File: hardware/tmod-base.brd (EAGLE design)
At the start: 65 x 56 mm, 100 parts, among them IC1 TPS70933, IC10 TPS70933, IC2 INA219SOT, IC3 STM32L052C8T6, IC4 HX1, IC5 LMP7702, IC6 TPS62143, IC8 TPS22918, IC9 BME280, J1 DNP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

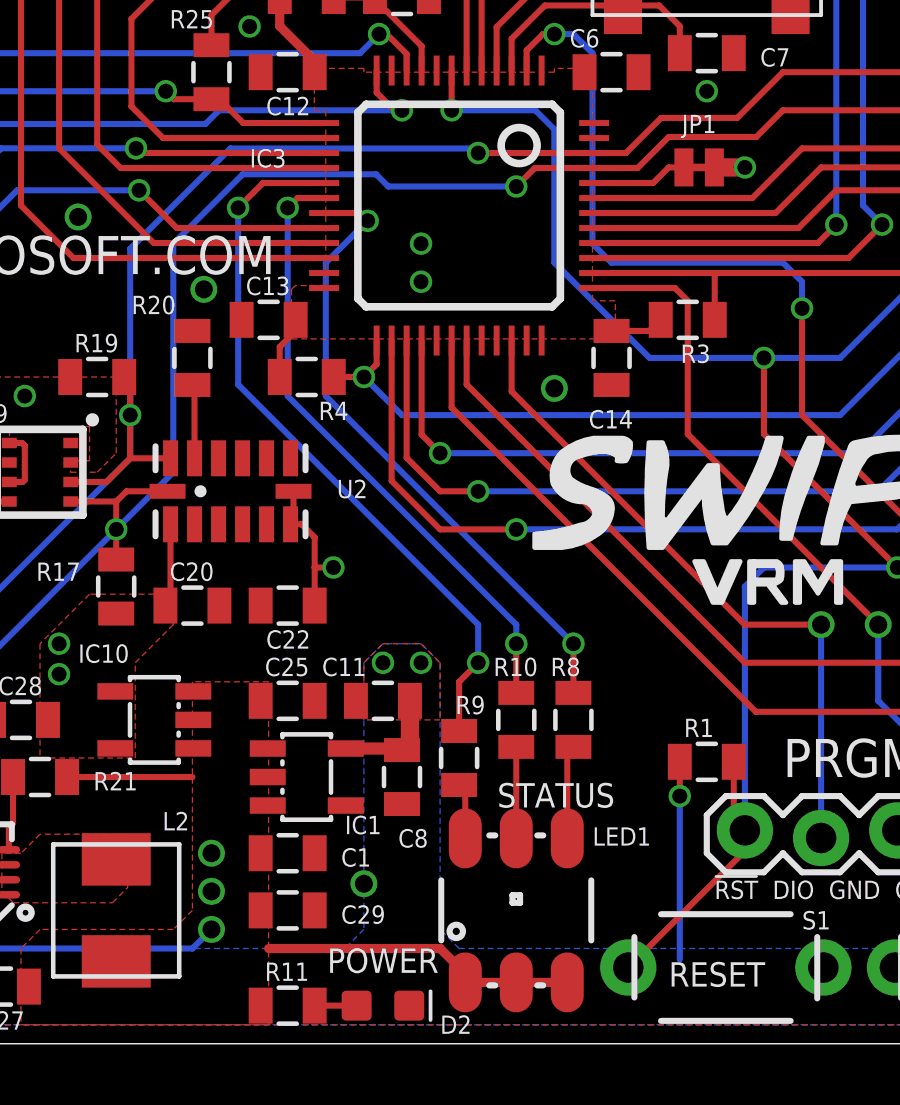
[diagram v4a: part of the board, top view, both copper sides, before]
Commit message: Rotate LED by 180 degrees to match the actual part
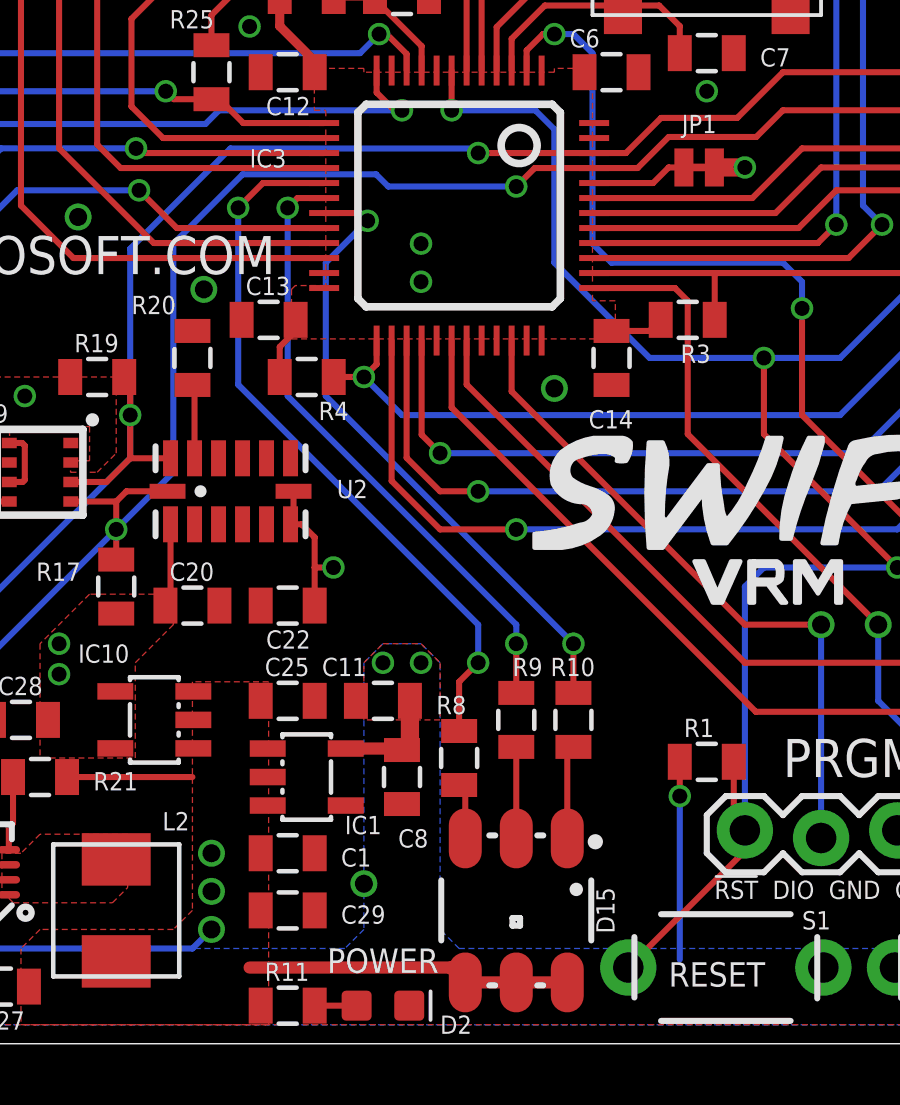
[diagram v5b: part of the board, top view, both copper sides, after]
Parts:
- removed LED1: STATUS, SparkFun-LED:LED-TRICOLOR-5050
- added D15: LED-RGB, HAB:LED-TRICOLOR-5050
- moved R8 4.02 mm to (35.6, 9.53)
- moved R9 2.29 mm to (37.5, 10.8)
- moved R10 1.90 mm to (39.4, 10.8)
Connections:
- net 5V: now also D15.4, D15.5, D15.6; no longer LED1.1, LED1.2, LED1.3
- net BC: now also D15.1, R10.2; no longer LED1.4, R8.2
- net GC: now also D15.2; no longer LED1.6
- net LEDB: now also R10.1; no longer R8.1
- net LEDG: now also IC3.18; no longer IC3.17
- net LEDR: now also IC3.17, R8.1; no longer IC3.18, R10.1
- net RC: now also D15.3, R8.2; no longer LED1.5, R10.2
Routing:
- net LEDR: track 20.7 -> 24.2 mm
- net LEDG: track 24.2 -> 20.7 mm
- net RC: track 3.05 -> 1.86 mm
- net GC: track 1.86 -> 3.05 mm
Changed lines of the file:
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@@
 <attribute name="VALUE" x="23.13" y="1.3462" size="0.6096" layer="27" ratio="15"/>
-</element>
-<element name="LED1" library="SparkFun-LED" package="LED-TRICOLOR-5050" value="STATUS" x="37.465" y="4.445" smashed="yes" rot="R90">
-<attribute name="NAME" x="40.005" y="6.604" size="0.6096" layer="25" ratio="15"/>
-<attribute name="VALUE" x="36.83" y="7.874" size="0.8128" layer="21"/>
 </element>
 <element name="R1" library="SparkFun-Passives" package="0805" value="10K" x="43.815" y="9.398" smashed="yes" rot="R180">
@@
 <attribute name="VALUE" x="42.799" y="8.001" size="0.6096" layer="27" ratio="15"/>
 </element>
-<element name="R10" library="SparkFun-Passives" package="0805" value="560" x="37.465" y="10.795" smashed="yes" rot="R270">
-<attribute name="NAME" x="36.703" y="12.2555" size="0.6096" layer="25" ratio="15"/>
-<attribute name="VALUE" x="37.084" y="8.763" size="0.6096" layer="27" ratio="15"/>
+<element name="R10" library="SparkFun-Passives" package="0805" value="560" x="39.37" y="10.795" smashed="yes" rot="R270">
+<attribute name="NAME" x="38.608" y="12.2555" size="0.6096" layer="25" ratio="15"/>
+<attribute name="VALUE" x="38.989" y="8.763" size="0.6096" layer="27" ratio="15"/>
 </element>
 <element name="R11" library="SparkFun-Passives" package="0805" value="3.3K" x="29.845" y="1.27" smashed="yes">
@@
 <attribute name="VALUE" x="19.177" y="15.494" size="0.6096" layer="27" ratio="15" rot="R90"/>
 </element>
-<element name="R8" library="SparkFun-Passives" package="0805" value="470" x="39.37" y="10.795" smashed="yes" rot="R270">
-<attribute name="NAME" x="38.608" y="12.2555" size="0.6096" layer="25" ratio="15"/>
-<attribute name="VALUE" x="38.989" y="8.763" size="0.6096" layer="27" ratio="15"/>
-</element>
-<element name="R9" library="SparkFun-Passives" package="0805" value="470" x="35.56" y="9.525" smashed="yes" rot="R270">
-<attribute name="NAME" x="35.433" y="10.9855" size="0.6096" layer="25" ratio="15"/>
-<attribute name="VALUE" x="35.179" y="9.398" size="0.6096" layer="27" ratio="15"/>
+<element name="R8" library="SparkFun-Passives" package="0805" value="470" x="35.56" y="9.525" smashed="yes" rot="R270">
+<attribute name="NAME" x="34.798" y="10.9855" size="0.6096" layer="25" ratio="15"/>
+<attribute name="VALUE" x="35.179" y="7.493" size="0.6096" layer="27" ratio="15"/>
+</element>
+<element name="R9" library="SparkFun-Passives" package="0805" value="470" x="37.465" y="10.795" smashed="yes" rot="R270">
+<attribute name="NAME" x="37.338" y="12.2555" size="0.6096" layer="25" ratio="15"/>
+<attribute name="VALUE" x="37.084" y="10.668" size="0.6096" layer="27" ratio="15"/>
 </element>
 <element name="S1" library="HAB" package="TACTILE-PTH-THIN" value="RST" x="44.45" y="2.54" smashed="yes" rot="R180">
@@
 <attribute name="VALUE" x="7.874" y="30.353" size="0.4064" layer="27"/>
 </element>
+<element name="D15" library="HAB" package="LED-TRICOLOR-5050" value="LED-RGB" x="37.465" y="4.445" rot="R270"/>
 </elements>
 <signals>
@@
 <contactref element="C16" pad="1"/>
 <contactref element="R6" pad="2"/>
-<contactref element="LED1" pad="3"/>
-<contactref element="LED1" pad="1"/>
-<contactref element="LED1" pad="2"/>
 <contactref element="R13" pad="2"/>
 <contactref element="IC5" pad="8"/>
@@
 <wire x1="41.245" y1="52.41" x2="41.275" y2="52.44" width="0.2032" layer="1"/>
 <wire x1="22.49" y1="8.89" x2="26.67" y2="8.89" width="0.2032" layer="1"/>
-<wire x1="35.765" y1="2.045" x2="37.465" y2="2.045" width="0.3048" layer="1"/>
-<wire x1="37.465" y1="2.045" x2="39.165" y2="2.045" width="0.3048" layer="1"/>
-<wire x1="35.765" y1="2.045" x2="35.765" y2="2.335" width="0.3048" layer="1"/>
-<wire x1="35.765" y1="2.335" x2="34.925" y2="3.175" width="0.3048" layer="1"/>
-<wire x1="34.925" y1="3.175" x2="29.21" y2="3.175" width="0.3048" layer="1"/>
 <wire x1="38.395" y1="52.41" x2="37.17" y2="52.41" width="0.2032" layer="1"/>
 <wire x1="37.17" y1="52.41" x2="36.83" y2="52.07" width="0.2032" layer="1"/>
@@
 <contactref element="J7" pad="A13"/>
 <contactref element="J7" pad="B3"/>
+<contactref element="D15" pad="6"/>
+<contactref element="D15" pad="5"/>
+<contactref element="D15" pad="4"/>
+<wire x1="39.165" y1="2.045" x2="35.765" y2="2.045" width="0.4064" layer="1"/>
+<wire x1="35.765" y1="2.045" x2="35.27" y2="2.54" width="0.4064" layer="1"/>
+<wire x1="35.27" y1="2.54" x2="28.575" y2="2.54" width="0.4064" layer="1"/>
+<wire x1="39.165" y1="2.045" x2="37.465" y2="2.045" width="0" layer="19" extent="1-1"/>
 </signal>
 <signal name="SCL">
@@
 <contactref element="U2" pad="9"/>
 </signal>
-<signal name="RC">
-<contactref element="R10" pad="2"/>
-<contactref element="LED1" pad="5"/>
-<wire x1="37.465" y1="6.845" x2="37.465" y2="9.895" width="0.2032" layer="1"/>
-</signal>
 <signal name="GC">
 <contactref element="R9" pad="2"/>
-<contactref element="LED1" pad="6"/>
-<wire x1="35.765" y1="6.845" x2="35.765" y2="8.42" width="0.2032" layer="1"/>
-<wire x1="35.765" y1="8.42" x2="35.56" y2="8.625" width="0.2032" layer="1"/>
+<contactref element="D15" pad="2"/>
+<wire x1="37.465" y1="6.845" x2="37.465" y2="9.895" width="0.2032" layer="1"/>
 </signal>
 <signal name="BC">
-<contactref element="LED1" pad="4"/>
-<contactref element="R8" pad="2"/>
-<wire x1="39.165" y1="6.845" x2="39.165" y2="9.69" width="0.2032" layer="1"/>
-<wire x1="39.165" y1="9.69" x2="39.37" y2="9.895" width="0.2032" layer="1"/>
+<contactref element="R10" pad="2"/>
+<contactref element="D15" pad="1"/>
+<wire x1="39.37" y1="9.895" x2="39.165" y2="9.69" width="0.2032" layer="1"/>
+<wire x1="39.165" y1="9.69" x2="39.165" y2="6.845" width="0.2032" layer="1"/>
 </signal>
 <signal name="LEDB">
-<contactref element="R8" pad="1"/>
-<contactref element="IC3" pad="19"/>
+<contactref element="R10" pad="1"/>
 <wire x1="39.37" y1="11.695" x2="39.37" y2="13.335" width="0.2032" layer="1"/>
 <via x="39.37" y="13.335" extent="1-16" drill="0.5"/>
 <wire x1="39.37" y1="13.335" x2="31.115" y2="21.59" width="0.2032" layer="16"/>
+<contactref element="IC3" pad="19"/>
 <via x="32.512" y="27.432" extent="1-16" drill="0.5"/>
 <wire x1="31.06" y1="27.69" x2="32.254" y2="27.69" width="0.2032" layer="1"/>
@@
 <signal name="LEDG">
 <contactref element="R9" pad="1"/>
-<contactref element="IC3" pad="17"/>
-<via x="36.195" y="12.7" extent="1-16" drill="0.5"/>
-<wire x1="36.195" y1="12.7" x2="36.195" y2="13.97" width="0.2032" layer="16"/>
-<wire x1="36.195" y1="13.97" x2="28.194" y2="21.971" width="0.2032" layer="16"/>
-<wire x1="28.194" y1="21.971" x2="28.194" y2="27.8638" width="0.2032" layer="16"/>
-<wire x1="35.56" y1="10.425" x2="35.56" y2="12.065" width="0.2032" layer="1"/>
-<wire x1="35.56" y1="12.065" x2="36.195" y2="12.7" width="0.2032" layer="1"/>
-<wire x1="29.0202" y1="28.69" x2="28.194" y2="27.8638" width="0.2032" layer="1"/>
-<via x="28.194" y="27.8638" extent="1-16" drill="0.5"/>
-<wire x1="31.06" y1="28.69" x2="29.0202" y2="28.69" width="0.2032" layer="1"/>
-</signal>
-<signal name="LEDR">
-<contactref element="R10" pad="1"/>
 <contactref element="IC3" pad="18"/>
+<wire x1="29.845" y1="21.59" x2="29.845" y2="27.8638" width="0.2032" layer="16"/>
+<via x="29.845" y="27.8638" extent="1-16" drill="0.5"/>
+<wire x1="31.06" y1="28.19" x2="30.1712" y2="28.19" width="0.2032" layer="1"/>
+<wire x1="30.1712" y1="28.19" x2="29.845" y2="27.8638" width="0.2032" layer="1"/>
 <wire x1="37.465" y1="11.695" x2="37.465" y2="13.335" width="0.2032" layer="1"/>
 <via x="37.465" y="13.335" extent="1-16" drill="0.5"/>
 <wire x1="37.465" y1="13.335" x2="37.465" y2="13.97" width="0.2032" layer="16"/>
 <wire x1="37.465" y1="13.97" x2="29.845" y2="21.59" width="0.2032" layer="16"/>
-<wire x1="29.845" y1="21.59" x2="29.845" y2="27.8638" width="0.2032" layer="16"/>
-<via x="29.845" y="27.8638" extent="1-16" drill="0.5"/>
-<wire x1="31.06" y1="28.19" x2="30.1712" y2="28.19" width="0.2032" layer="1"/>
-<wire x1="30.1712" y1="28.19" x2="29.845" y2="27.8638" width="0.2032" layer="1"/>
+</signal>
+<signal name="LEDR">
+<contactref element="R8" pad="1"/>
+<wire x1="35.56" y1="10.425" x2="35.56" y2="12.065" width="0.2032" layer="1"/>
+<wire x1="35.56" y1="12.065" x2="36.195" y2="12.7" width="0.2032" layer="1"/>
+<via x="36.195" y="12.7" extent="1-16" drill="0.5"/>
+<wire x1="36.195" y1="12.7" x2="36.195" y2="13.97" width="0.2032" layer="16"/>
+<wire x1="36.195" y1="13.97" x2="28.194" y2="21.971" width="0.2032" layer="16"/>
+<contactref element="IC3" pad="17"/>
+<via x="28.194" y="27.8638" extent="1-16" drill="0.5"/>
+<wire x1="28.194" y1="27.8638" x2="29.0202" y2="28.69" width="0.2032" layer="1"/>
+<wire x1="29.0202" y1="28.69" x2="31.06" y2="28.69" width="0.2032" layer="1"/>
+<wire x1="28.194" y1="21.971" x2="28.194" y2="27.8638" width="0.2032" layer="16"/>
 </signal>
 <signal name="TXD">
@@
 <wire x1="20.828" y1="28.448" x2="19.685" y2="27.305" width="0.2032" layer="16"/>
 </signal>
+<signal name="RC">
+<contactref element="R8" pad="2"/>
+<contactref element="D15" pad="3"/>
+<wire x1="35.56" y1="8.625" x2="35.765" y2="8.42" width="0.2032" layer="1"/>
+<wire x1="35.765" y1="8.42" x2="35.765" y2="6.845" width="0.2032" layer="1"/>
+</signal>
 </signals>

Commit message: Start work on new automated base station. Add BOM for Pi application board. Fix mirrored INA219 footprint and LED on base board
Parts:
- IC3: value STM32L052C8T6 -> STM32L443CCT6
- moved R22 5.08 mm to (10.2, 2.54)
- moved IC2 2.54 mm to (10.8, 6.35)
- moved C10 2.01 mm to (13.3, 5.71), turned to 90 degrees
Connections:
- net 3.3V: now also IC2.4; no longer IC2.5
- net GND: now also IC2.3, IC2.7, IC2.8; no longer IC2.1, IC2.2, IC2.6
- net SCL: now also IC2.5; no longer IC2.4
- net SDA: now also IC2.6; no longer IC2.3
- net VBAT: now also IC2.2; no longer IC2.7
- net VIN: now also IC2.1; no longer IC2.8
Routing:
- net SDA: track 78.4 -> 72.5 mm
- net SCL: track 76.8 -> 71.1 mm
- net 3.3V: track 30.5 -> 29.8 mm
- net GND: vias 21 -> 22
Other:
- board text added: "Maker Garage Project Phoenix REV C"
- board text removed: "Maker Garage Project Phoenix REV B"
